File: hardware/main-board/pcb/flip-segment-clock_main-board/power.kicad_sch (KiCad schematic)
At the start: 1 part

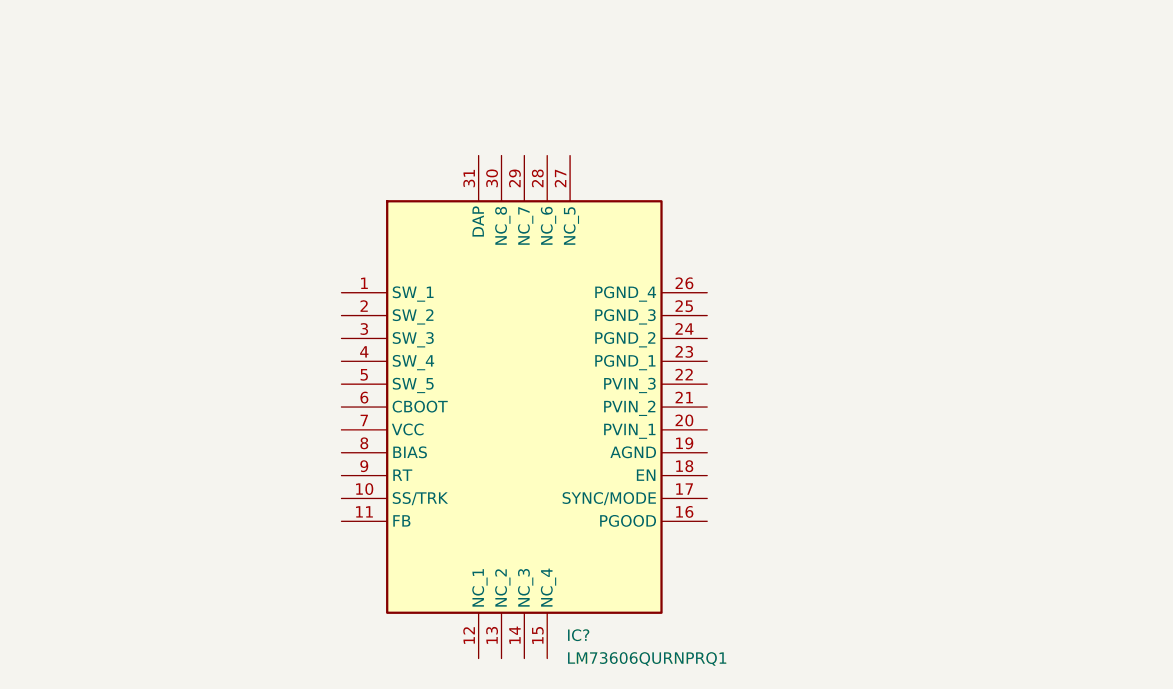
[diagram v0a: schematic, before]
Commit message: Refining design of the segment drivers
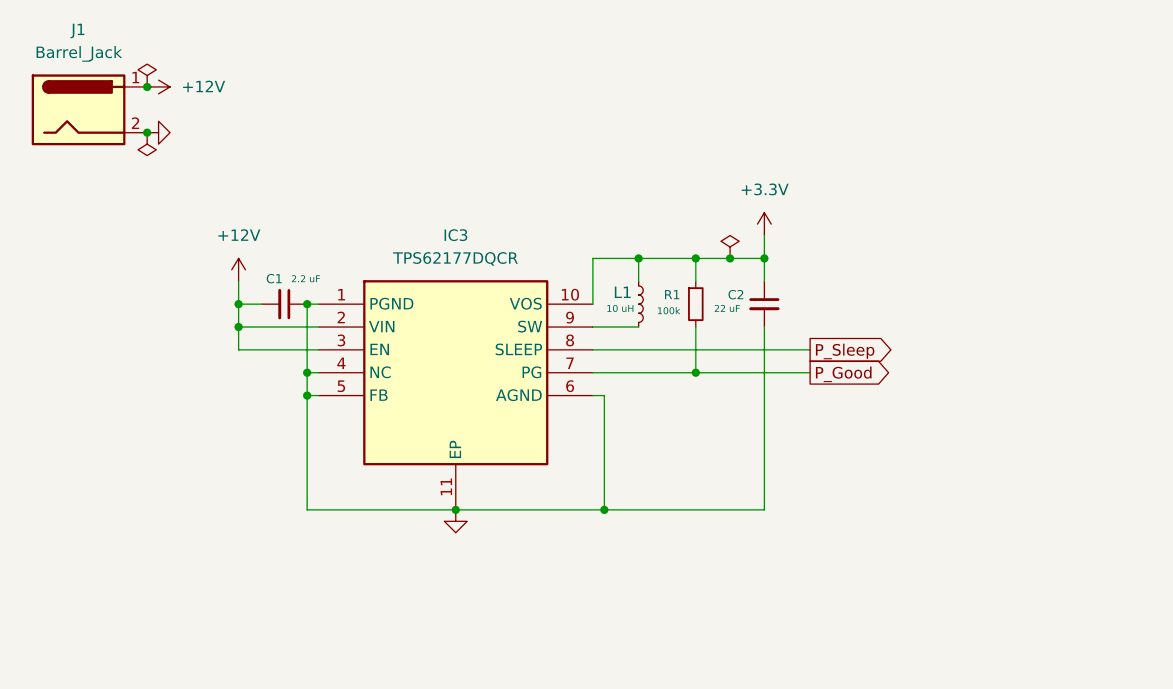
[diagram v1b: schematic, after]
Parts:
- removed IC?: LM73606QURNPRQ1, SamacSys_Parts:QFN50P400X600X80-31N-D, symbol SamacSys_Parts:LM73606QURNPRQ1
- added C1: 2.2 uF, Capacitor_SMD:C_0402_1005Metric, symbol Device:C_Small
- added C2: 22 uF, Capacitor_SMD:C_0402_1005Metric, symbol Device:C_Small
- added IC3: TPS62177DQCR, SamacSys_Parts:SON50P200X300X80-11N, symbol SamacSys_Parts:TPS62177DQCR
- added J1: Barrel_Jack, Connector_BarrelJack:BarrelJack_SwitchcraftConxall_RAPC10U_Horizontal, symbol Connector:Barrel_Jack
- added L1: 10 uH, Inductor_SMD:L_Coilcraft_LPS4018, symbol Device:L_Small
- added R1: 100k, Resistor_SMD:R_0402_1005Metric, symbol Device:R_Small
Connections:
- new net: IC3.9 (SW), L1.2
- new net +12V: C1.2, IC3.2 (VIN), IC3.3 (EN), J1.1
- new net +3.3V: C2.1, IC3.10 (VOS), L1.1, R1.1
- new net GND: C1.1, C2.2, IC3.1 (PGND), IC3.11 (EP), IC3.4 (NC), IC3.5 (FB), IC3.6 (AGND), J1.2
- new net P_Good: IC3.7 (PG), R1.2
- new net P_Sleep: IC3.8 (SLEEP)

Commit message: Unsure
Unsure of previous changes due to time off. Currently edited the lessons learned page.
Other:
- moved on the sheet: C1, C2, IC3, J1, L1, R1
